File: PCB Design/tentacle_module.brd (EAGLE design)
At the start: 100 x 80 mm, 40 parts, among them IC1 5V, X3 RJ45-8X, X4 RJ45-8X

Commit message: fixed the indicator LED error.
The negative pin of the LED was connected to the ground and the positive
pin was connected to the drain. That wouldn't have worked.
Also rotated the longer labels to make them fit nicer.
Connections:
- removed net GND_TEST: JP1.1, R10.1, R11.1, R12.1, R9.1
- removed net SMA1_OUT-1: LED2.A
- removed net SMA1_OUT-2: LED3.A
- removed net SMA1_OUT-3: LED4.A
- new net LED_TEST: LED2.A, LED3.A, LED4.A
- new net TEST_LED: JP1.3, LED1.A
- net +5V: now also JP1.2
- net GND: no longer JP1.2
- net SMA1_OUT-: now also R9.1; no longer LED1.A
- net SMA2_OUT-: now also R10.1
- net SMA3_OUT-: now also R11.1
- net SMA4_OUT-: now also R12.1
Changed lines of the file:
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@@
 <contactref element="JP2" pad="1"/>
 <contactref element="JP2" pad="3"/>
+<contactref element="JP1" pad="2"/>
 <wire x1="-51.435" y1="35.56" x2="-97.79" y2="-2.54" width="0" layer="19" extent="1-1"/>
 <wire x1="-33.15" y1="54.61" x2="-51.435" y2="35.56" width="0" layer="19" extent="1-1"/>
-<wire x1="-175.26" y1="-171.45" x2="-97.79" y2="-2.54" width="0" layer="19" extent="1-1"/>
+<wire x1="-165.1" y1="-171.45" x2="-97.79" y2="-2.54" width="0" layer="19" extent="1-1"/>
+<wire x1="-175.26" y1="-171.45" x2="-165.1" y2="-171.45" width="0" layer="19" extent="1-1"/>
 <wire x1="-180.34" y1="-171.45" x2="-175.26" y2="-171.45" width="0" layer="19" extent="1-1"/>
 </signal>
@@
 <contactref element="R7" pad="1"/>
 <contactref element="C5" pad="2"/>
-<contactref element="JP1" pad="2"/>
 <contactref element="X2" pad="2"/>
 <contactref element="JP3" pad="2"/>
@@
 <wire x1="-30.35" y1="54.61" x2="-35.56" y2="46.97" width="0" layer="19" extent="1-1"/>
 <wire x1="-20.32" y1="46.97" x2="-30.35" y2="54.61" width="0" layer="19" extent="1-1"/>
-<wire x1="-165.1" y1="-171.45" x2="-136.042" y2="-104.14" width="0" layer="19" extent="1-1"/>
-<wire x1="-190.5" y1="-182.88" x2="-165.1" y2="-171.45" width="0" layer="19" extent="1-1"/>
+<wire x1="-190.5" y1="-182.88" x2="-136.042" y2="-104.14" width="0" layer="19" extent="1-1"/>
 <wire x1="-218.44" y1="-223.52" x2="-190.5" y2="-182.88" width="0" layer="19" extent="1-1"/>
 <wire x1="-228.6" y1="-223.52" x2="-218.44" y2="-223.52" width="0" layer="19" extent="1-1"/>
@@
 <contactref element="T1" pad="2"/>
 <contactref element="X5" pad="2"/>
-<contactref element="LED1" pad="A"/>
+<contactref element="R9" pad="1"/>
 <wire x1="-67.31" y1="8.85" x2="-110.53" y2="-6.35" width="0" layer="19" extent="1-1"/>
-<wire x1="-143.03" y1="-120.65" x2="-110.53" y2="-6.35" width="0" layer="19" extent="1-1"/>
+<wire x1="-147.472" y1="-137.16" x2="-110.53" y2="-6.35" width="0" layer="19" extent="1-1"/>
 </signal>
 <signal name="N$4">
@@
 <contactref element="T2" pad="2"/>
 <contactref element="X6" pad="2"/>
+<contactref element="R10" pad="1"/>
 <wire x1="-142.24" y1="-36.87" x2="-139.74" y2="-50.8" width="0" layer="19" extent="1-1"/>
+<wire x1="-147.472" y1="-143.51" x2="-139.74" y2="-50.8" width="0" layer="19" extent="1-1"/>
 </signal>
 <signal name="N$2">
@@
 <wire x1="-146.53" y1="-120.65" x2="-144.628" y2="-137.16" width="0" layer="19" extent="1-1"/>
 </signal>
-<signal name="SMA1_OUT-1">
-<contactref element="LED2" pad="A"/>
-</signal>
 <signal name="N$6">
 <contactref element="LED2" pad="C"/>
@@
 <wire x1="-144.628" y1="-143.51" x2="-146.53" y2="-149.86" width="0" layer="19" extent="1-1"/>
 </signal>
-<signal name="SMA1_OUT-2">
-<contactref element="LED3" pad="A"/>
-</signal>
 <signal name="N$7">
 <contactref element="LED3" pad="C"/>
@@
 <wire x1="-144.628" y1="-154.94" x2="-146.53" y2="-161.29" width="0" layer="19" extent="1-1"/>
 </signal>
-<signal name="SMA1_OUT-3">
-<contactref element="LED4" pad="A"/>
-</signal>
 <signal name="N$8">
 <contactref element="LED4" pad="C"/>
@@
 <contactref element="T3" pad="2"/>
 <contactref element="X7" pad="2"/>
+<contactref element="R11" pad="1"/>
 <wire x1="-142.24" y1="-64.81" x2="-139.74" y2="-78.74" width="0" layer="19" extent="1-1"/>
+<wire x1="-147.472" y1="-154.94" x2="-139.74" y2="-78.74" width="0" layer="19" extent="1-1"/>
 </signal>
 <signal name="SMA4_OUT-">
 <contactref element="T4" pad="2"/>
 <contactref element="X8" pad="2"/>
+<contactref element="R12" pad="1"/>
 <wire x1="-142.24" y1="-92.75" x2="-139.74" y2="-106.68" width="0" layer="19" extent="1-1"/>
-</signal>
-<signal name="GND_TEST">
-<contactref element="R11" pad="1"/>
-<contactref element="R12" pad="1"/>
-<contactref element="JP1" pad="1"/>
-<contactref element="R9" pad="1"/>
-<contactref element="R10" pad="1"/>
-<wire x1="-147.472" y1="-166.37" x2="-167.64" y2="-171.45" width="0" layer="19" extent="1-1"/>
-<wire x1="-147.472" y1="-154.94" x2="-147.472" y2="-166.37" width="0" layer="19" extent="1-1"/>
-<wire x1="-147.472" y1="-143.51" x2="-147.472" y2="-154.94" width="0" layer="19" extent="1-1"/>
-<wire x1="-147.472" y1="-137.16" x2="-147.472" y2="-143.51" width="0" layer="19" extent="1-1"/>
+<wire x1="-147.472" y1="-166.37" x2="-139.74" y2="-106.68" width="0" layer="19" extent="1-1"/>
+</signal>
+<signal name="LED_TEST">
+<contactref element="LED2" pad="A"/>
+<contactref element="LED3" pad="A"/>
+<contactref element="LED4" pad="A"/>
+<wire x1="-143.03" y1="-161.29" x2="-143.03" y2="-172.72" width="0" layer="19" extent="1-1"/>
+<wire x1="-143.03" y1="-149.86" x2="-143.03" y2="-161.29" width="0" layer="19" extent="1-1"/>
 </signal>
 <signal name="+5V_HI-PWR">
@@
 <wire x1="-177.8" y1="-171.45" x2="-144.74" y2="-106.68" width="0" layer="19" extent="1-1"/>
 </signal>
+<signal name="TEST_LED">
+<contactref element="LED1" pad="A"/>
+<contactref element="JP1" pad="3"/>
+<wire x1="-143.03" y1="-120.65" x2="-162.56" y2="-171.45" width="0" layer="19" extent="1-1"/>
+</signal>
 </signals>

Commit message: Tentacle board improvement
Added Schottky diodes for reverse voltage protection
Added headers fro the RJ45 jack for more flexibility in terms of
connectors
Added modified the appearance of the schematic and added some more
comments.
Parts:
- removed LED2, LED3, LED4: (no value), led:SML1206
- removed R10, R11, R12: 470, rcl:R1206
- added D1, D2: SB540E-G, CBLA_Test_bed_Library:DO201T15
- added JP4, JP7: (no value), jumper:JP2W
- added LED5, LED6, LED7, LED8, LED9: (no value), led:SML1206
- added R13, R14, R15, R16, R17: 470, rcl:R1206
- added X10, X12, X13, X9: (no value), pinhead:1X08/90
- moved X6 327.3 mm to (-243.8, -360.7)
- moved X7 320.1 mm to (-243.8, -381.0)
- moved X8 303.3 mm to (-243.8, -391.2)
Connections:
- removed net LED_TEST: LED2.A, LED3.A, LED4.A
- removed net N$6: LED2.C, R10.2
- removed net N$7: LED3.C, R11.2
- removed net N$8: LED4.C, R12.2
- removed net TEST_LED: JP1.3, LED1.A
- new net +12V1: JP7.2
- new net GND1: R14.1
- new net N$10: LED5.C, R13.2
- new net N$11: JP4.3, LED5.A
- new net N$12: LED6.C, R14.2
- new net N$13: JP7.3, LED6.A
- new net N$14: LED7.C, R15.2
- new net N$15: LED8.C, R16.2
- new net N$16: LED9.C, R17.2
- new net TEST_LED_V+: JP1.3, LED1.A, LED7.A, LED8.A, LED9.A
- net +12V: now also D1.C, JP4.2
- net +3.3V: now also X12.1, X13.1
- net +5V: now also X12.3, X13.3
- net +5V_SW-REG: now also D2.C
- net GND: now also D1.A, D2.A, R13.1, X12.2, X13.2
- net IR1: now also X10.5, X9.5
- net IR2: now also X10.6, X12.4, X13.4, X9.6
- net PWM1: now also X10.1, X9.1
- net PWM2: now also X10.2, X9.2
- net PWM3: now also X10.3, X9.3
- net PWM4: now also X10.4, X9.4
- net SCL: now also X10.7, X12.6, X13.6, X9.7
- net SDA: now also X10.8, X12.5, X13.5, X9.8
- net SMA2_OUT-: now also R15.1; no longer R10.1
- net SMA3_OUT-: now also R16.1; no longer R11.1
- net SMA4_OUT-: now also R17.1; no longer R12.1

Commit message: Positioned components on Tentacle PCB
Fixed some mistakes on the schematics
Remove one pair of the headers for the RJ45 port
Placed  components on the PCB.
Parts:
- removed X10, X13: (no value), pinhead:1X08/90
- removed X11: (no value), con-wago-500:W237-103
- C2: device rcl:C1210 -> rcl:C1206
- IC1, IC2: device CBLA_Test_bed_Library:78XXS -> CBLA_Test_bed_Library:TO220L1
- JP1, JP2, JP4, JP7: device jumper:JP2W -> jumper:JP2
- T1, T2, T3, T4: value (none) -> NTD5867NL
- X1: device con-wago-500:W237-103 -> con-wago-508:W237-4P
- X2: device con-wago-500:W237-103 -> con-wago-508:W237-133
- moved LED9 526.2 mm to (80.0, 6.35)
- moved LED8 525.3 mm to (80.0, 16.5)
- moved R17 523.2 mm to (80.0, 8.89), turned to 180 degrees
- moved X8 518.6 mm to (87.6, 7.62), turned to 90 degrees
- moved X7 518.6 mm to (87.6, 17.8), turned to 90 degrees
- moved LED7 518.3 mm to (80.0, 26.7)
- moved R16 516.9 mm to (80.0, 19.1)
- moved R15 515.3 mm to (80.0, 29.2), turned to 180 degrees
- moved X6 510.8 mm to (87.6, 27.9), turned to 90 degrees
- moved JP7 465.8 mm to (24.1, 34.3), turned to 180 degrees
- moved R14 457.7 mm to (10.2, 26.0), turned to 180 degrees
- moved D2 457.7 mm to (22.9, 40.6)
- moved LED6 450.7 mm to (3.81, 26.0), turned to 180 degrees
- moved X12 439.8 mm to (71.1, 34.3), turned to 90 degrees
- moved JP4 438.7 mm to (24.1, 22.9), turned to 180 degrees
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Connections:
- net +12V: now also IC1.1, IC2.1; no longer IC1.IN, IC2.IN, X1.3, X11.1, X11.3
- net +3.3V: no longer X13.1
- net +3V3: now also IC2.3; no longer IC2.OUT
- net +5V: now also IC1.3; no longer IC1.OUT, X13.3
- net GND: now also IC1.2, IC2.2, X1.3; no longer IC1.GND, IC2.GND, X11.2, X13.2
- net IR1: no longer X10.5
- net IR2: no longer X10.6, X13.4
- net PWM1: no longer X10.1
- net PWM2: no longer R6.1, R8.1, X10.2
- net PWM3: now also R6.1; no longer X10.3
- net PWM4: now also R8.1; no longer X10.4
- net SCL: no longer X10.7, X13.6
- net SDA: no longer X10.8, X13.5
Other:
- board size 100 x 80 mm -> 94 x 44.5 mm

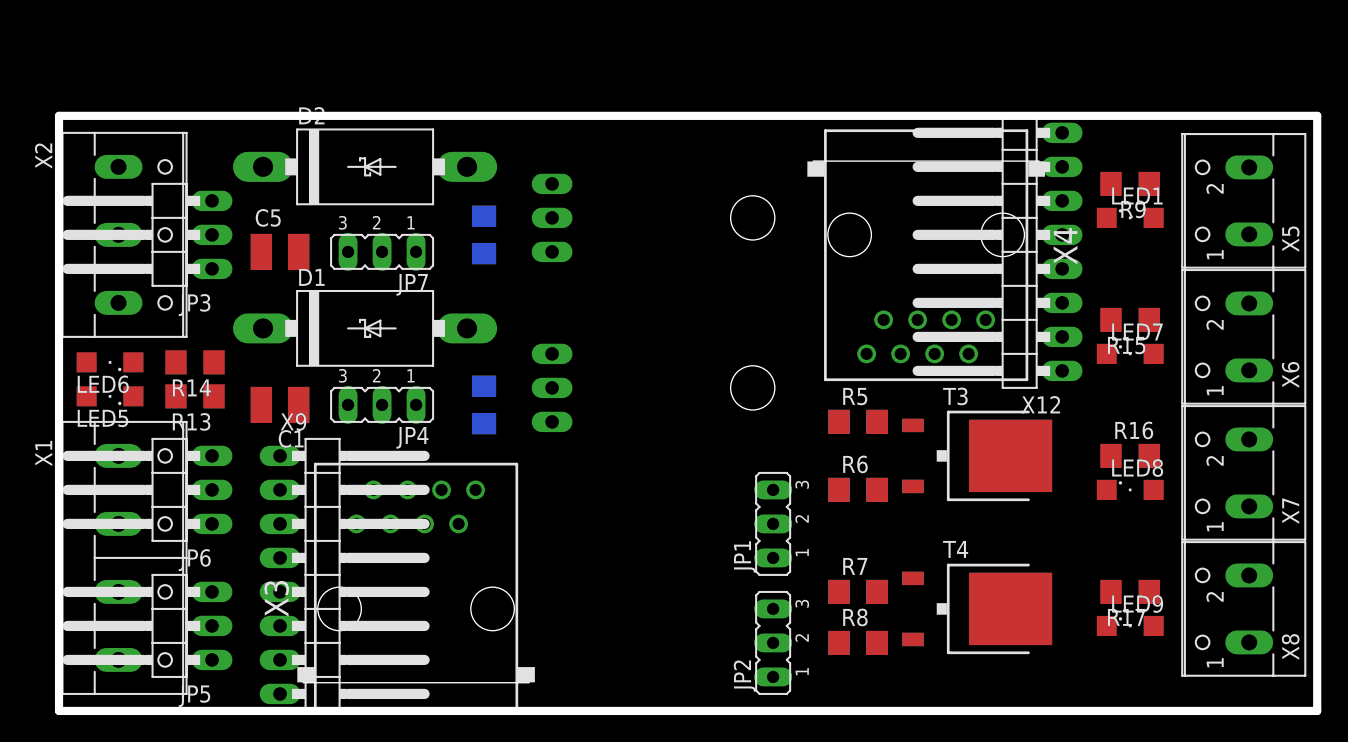
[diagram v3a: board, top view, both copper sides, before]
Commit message: Added mounting holes to Tentacle PCB
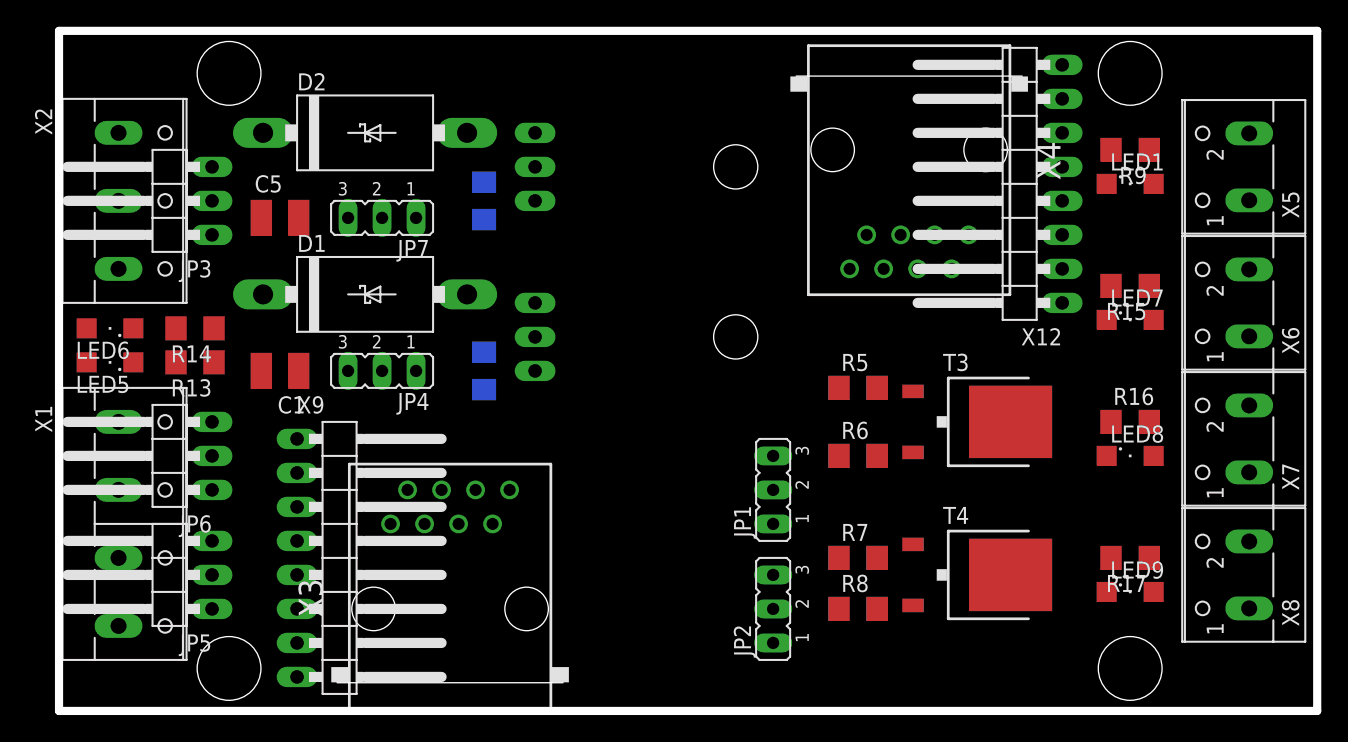
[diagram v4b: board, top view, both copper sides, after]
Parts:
- moved X4 6.48 mm to (63.5, 41.9)
- moved X12 5.08 mm to (71.1, 39.4)
- moved IC1 4.02 mm to (39.4, 27.9)
- moved IC2 4.02 mm to (39.4, 40.6)
- moved JP5 3.81 mm to (7.62, 10.2)
- moved JP1 2.54 mm to (53.3, 16.5)
- moved LED9 2.54 mm to (80.0, 8.89)
- moved X1 2.54 mm to (5.08, 14.0)
- moved JP2 2.54 mm to (53.3, 7.62)
- moved R2 2.54 mm to (59.7, 7.62)
- moved R8 2.54 mm to (59.7, 7.62)
- moved T2 2.54 mm to (68.6, 10.2)
- moved T4 2.54 mm to (68.6, 10.2)
- moved X8 2.54 mm to (87.6, 10.2)
- moved C1 2.54 mm to (16.5, 25.4)
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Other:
- board size 94 x 44.5 mm -> 94 x 50.8 mm

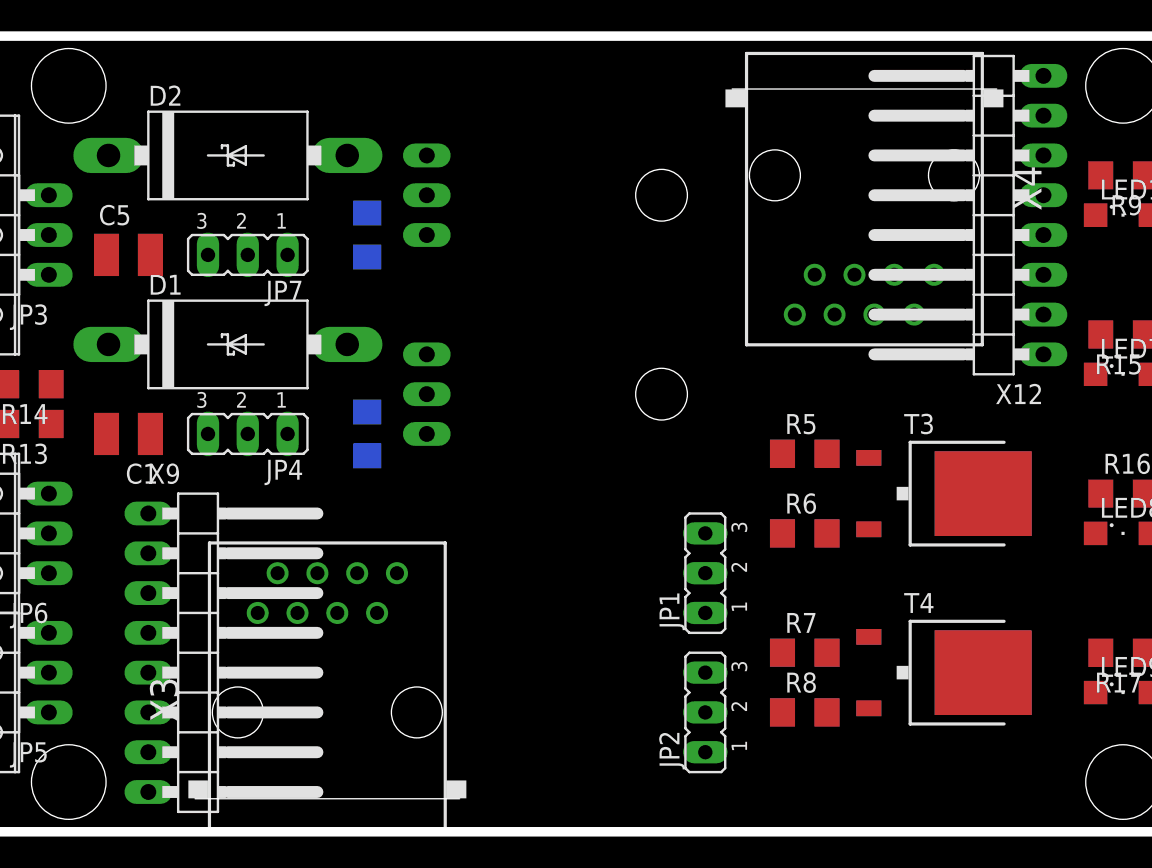
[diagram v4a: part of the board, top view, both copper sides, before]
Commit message: Changed capacitor footprint from 1210 to 1206
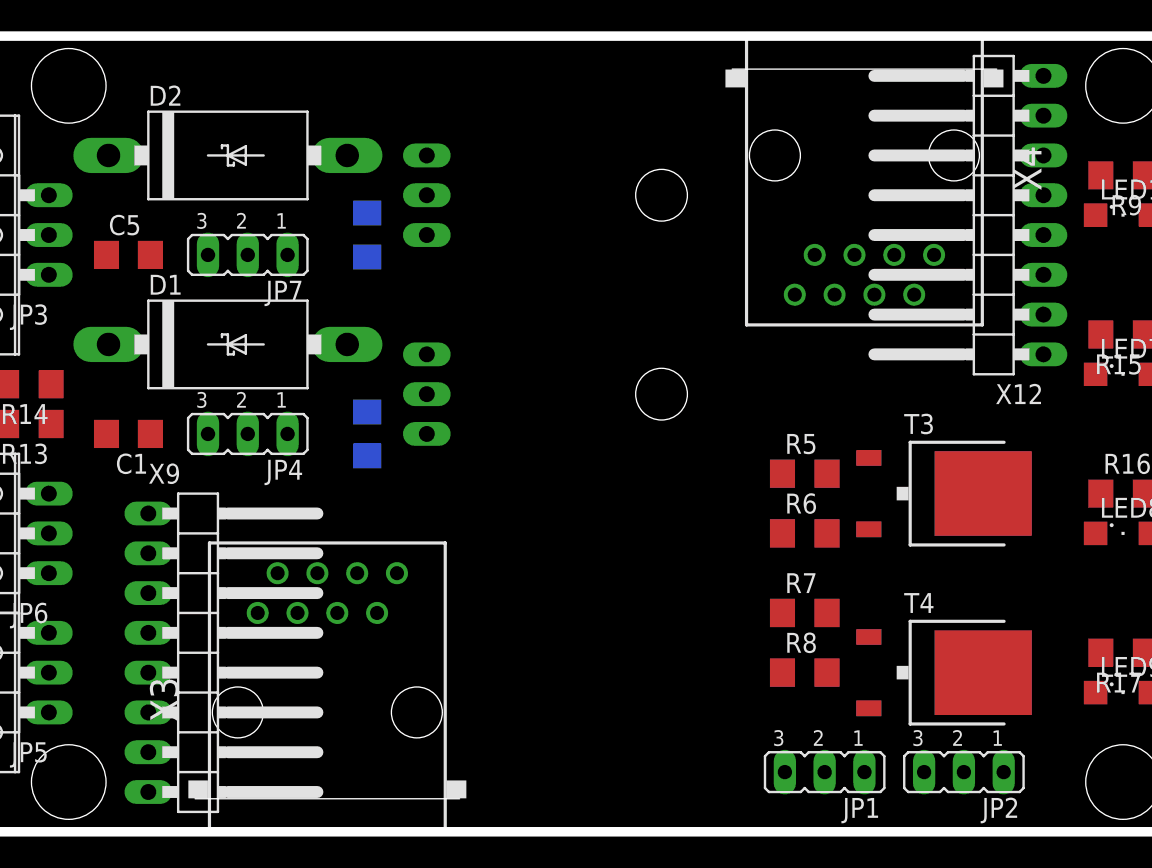
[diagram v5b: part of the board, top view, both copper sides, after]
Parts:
- C1, C5: device rcl:C1210 -> rcl:C1206
- moved JP2 16.9 mm to (69.8, 3.81), turned to 180 degrees
- moved JP1 14.8 mm to (61.0, 3.81), turned to 180 degrees
- moved R4 2.54 mm to (59.7, 14.0)
- moved R7 2.54 mm to (59.7, 14.0)
- moved R2 2.54 mm to (59.7, 10.2)
- moved R8 2.54 mm to (59.7, 10.2)
- moved X4 1.27 mm to (63.5, 43.2)
- moved R3 1.27 mm to (59.7, 22.9)
- moved R5 1.27 mm to (59.7, 22.9)
